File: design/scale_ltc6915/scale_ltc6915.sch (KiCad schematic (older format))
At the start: 0 parts

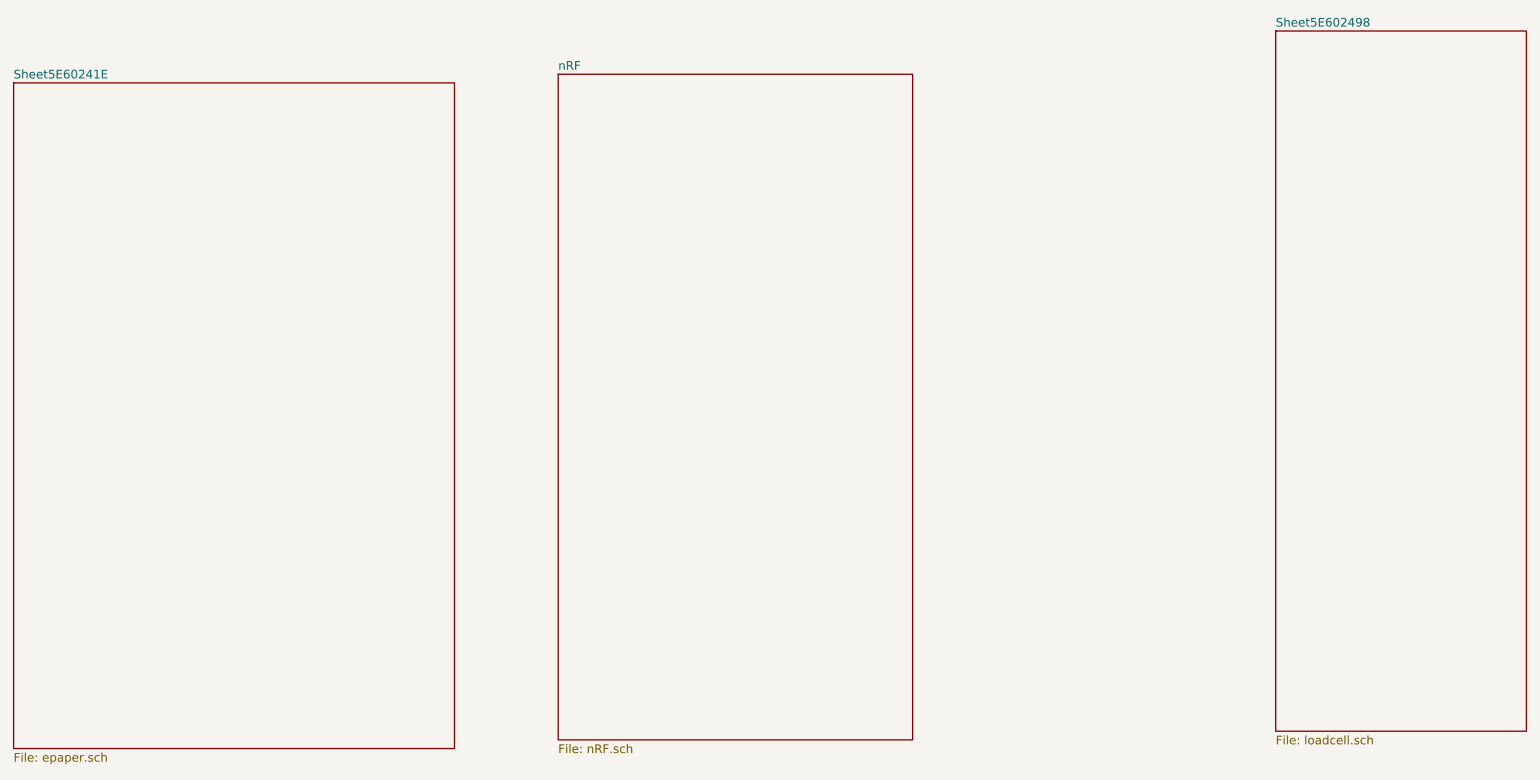
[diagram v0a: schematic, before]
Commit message: updated schematic of scale_ltc6915, fixed issues
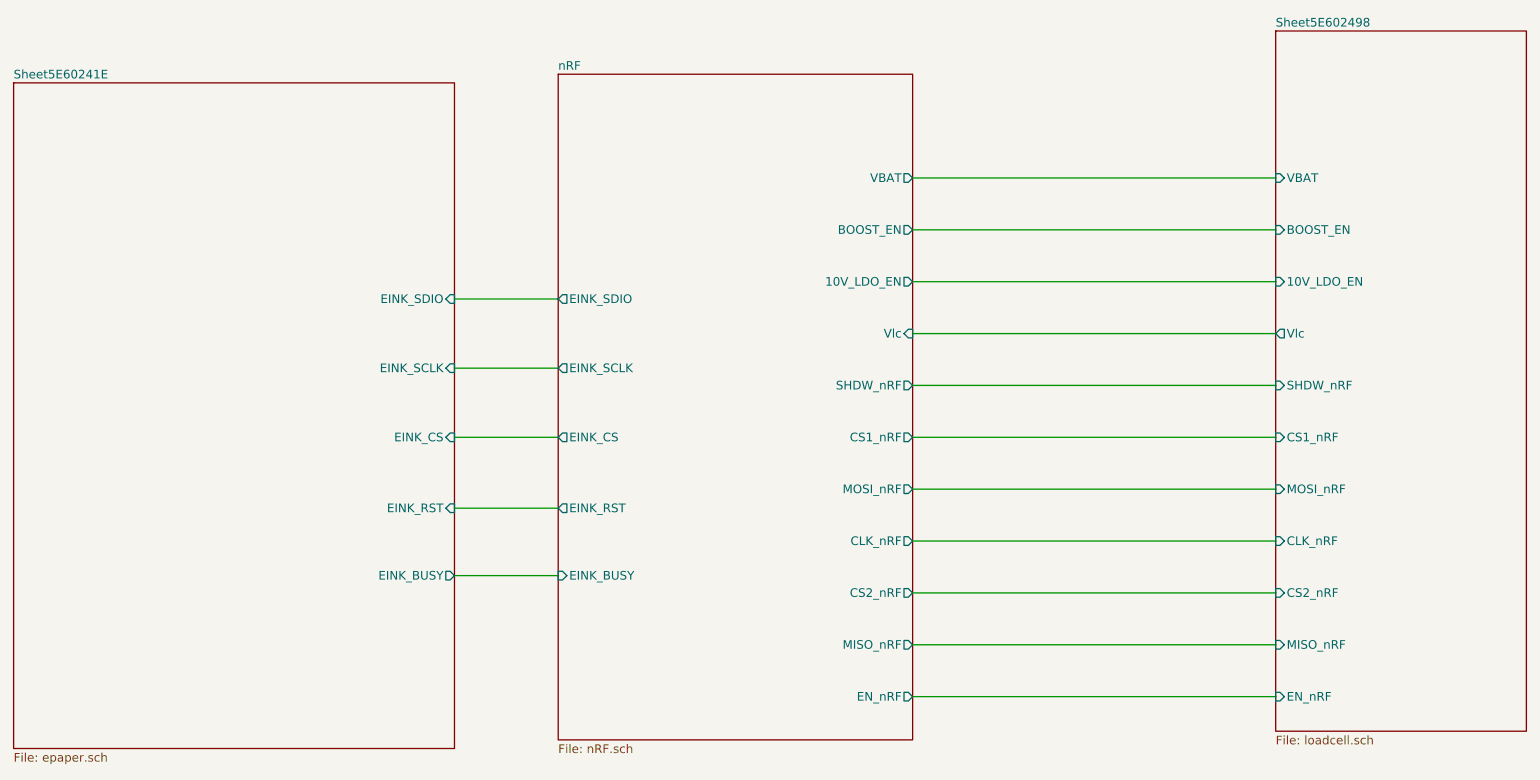
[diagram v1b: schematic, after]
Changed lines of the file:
@@
 F0 "nRF" 50
 F1 "nRF.sch" 50
+F2 "EINK_SDIO" O L 4400 3300 50
+F3 "EINK_SCLK" O L 4400 3700 50
+F4 "EINK_CS" O L 4400 4100 50
+F5 "EINK_RST" O L 4400 4510 50
+F6 "EINK_BUSY" I L 4400 4900 50
+F7 "VBAT" O R 6450 2600 50
+F8 "BOOST_EN" O R 6450 2900 50
+F9 "10V_LDO_EN" O R 6450 3200 50
+F10 "Vlc" I R 6450 3500 50
+F11 "SHDW_nRF" O R 6450 3800 50
+F12 "CS1_nRF" O R 6450 4100 50
+F13 "MOSI_nRF" O R 6450 4400 50
+F14 "CLK_nRF" O R 6450 4700 50
+F15 "CS2_nRF" O R 6450 5000 50
+F16 "MISO_nRF" O R 6450 5300 50
+F17 "EN_nRF" O R 6450 5600 50
 $EndSheet
 $Sheet
@@
 F0 "Sheet5E60241E" 50
 F1 "epaper.sch" 50
+F2 "EINK_SDIO" I R 3800 3300 50
+F3 "EINK_SCLK" I R 3800 3700 50
+F4 "EINK_CS" I R 3800 4100 50
+F5 "EINK_RST" I R 3800 4510 50
+F6 "EINK_BUSY" O R 3800 4900 50
 $EndSheet
+Wire Wire Line
+	3800 3300 4400 3300
+Wire Wire Line
+	4400 3700 3800 3700
+Wire Wire Line
+	3800 4100 4400 4100
+Wire Wire Line
+	3800 4510 4400 4510
+Wire Wire Line
+	4400 4900 3800 4900
 $Sheet
 S 8550 1750 1450 4050
@@
 F0 "Sheet5E602498" 50
 F1 "loadcell.sch" 50
+F2 "VBAT" I L 8550 2600 50
+F3 "BOOST_EN" I L 8550 2900 50
+F4 "10V_LDO_EN" I L 8550 3200 50
+F5 "Vlc" O L 8550 3500 50
+F6 "SHDW_nRF" I L 8550 3800 50
+F7 "CS1_nRF" I L 8550 4100 50
+F8 "MOSI_nRF" I L 8550 4400 50
+F9 "CLK_nRF" I L 8550 4700 50
+F10 "CS2_nRF" I L 8550 5000 50
+F11 "MISO_nRF" I L 8550 5300 50
+F12 "EN_nRF" I L 8550 5600 50
 $EndSheet
+Wire Wire Line
+	6450 5600 8550 5600
+Wire Wire Line
+	8550 5300 6450 5300
+Wire Wire Line
+	6450 5000 8550 5000
+Wire Wire Line
+	8550 4700 6450 4700
+Wire Wire Line
+	6450 4400 8550 4400
+Wire Wire Line
+	8550 4100 6450 4100
+Wire Wire Line
+	8550 3800 6450 3800
+Wire Wire Line
+	6450 3500 8550 3500
+Wire Wire Line
+	8550 3200 6450 3200
+Wire Wire Line
+	6450 2900 8550 2900
+Wire Wire Line
+	8550 2600 6450 2600
 $EndSCHEMATC

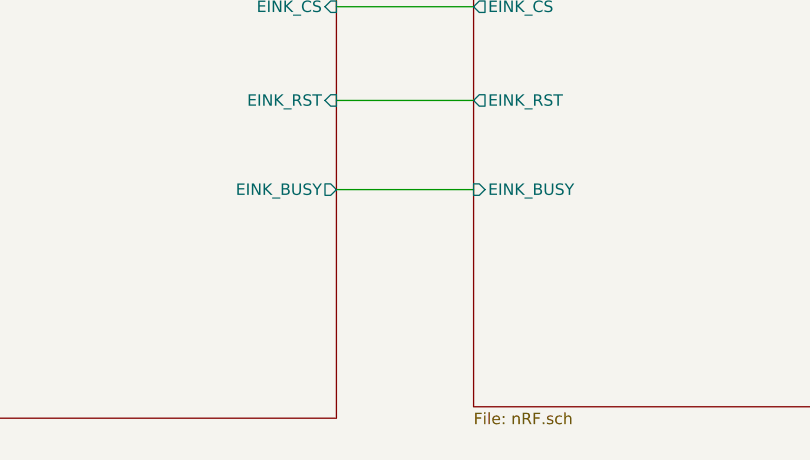
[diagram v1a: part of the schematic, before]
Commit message: DC, CS pins separated, issue fixed. In both scale_hx711 and scale_ltc6915.
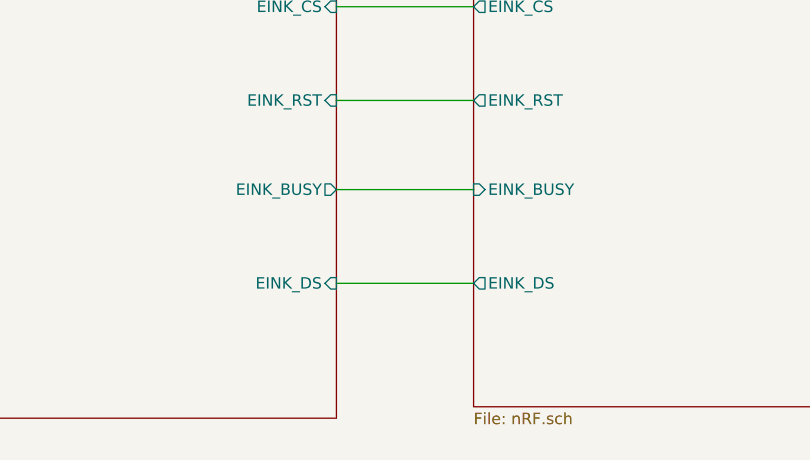
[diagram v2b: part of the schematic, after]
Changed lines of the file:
@@
 F16 "MISO_nRF" O R 6450 5300 50
 F17 "EN_nRF" O R 6450 5600 50
+F18 "EINK_DS" O L 4400 5310 50
 $EndSheet
 $Sheet
@@
 F5 "EINK_RST" I R 3800 4510 50
 F6 "EINK_BUSY" O R 3800 4900 50
+F7 "EINK_DS" I R 3800 5310 50
 $EndSheet
 Wire Wire Line
@@
 Wire Wire Line
 	8550 2600 6450 2600
+Wire Wire Line
+	3800 5310 4400 5310
 $EndSCHEMATC
